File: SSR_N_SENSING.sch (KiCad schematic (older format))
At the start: 15 parts, among them Q1 BC850, U3 ACS722

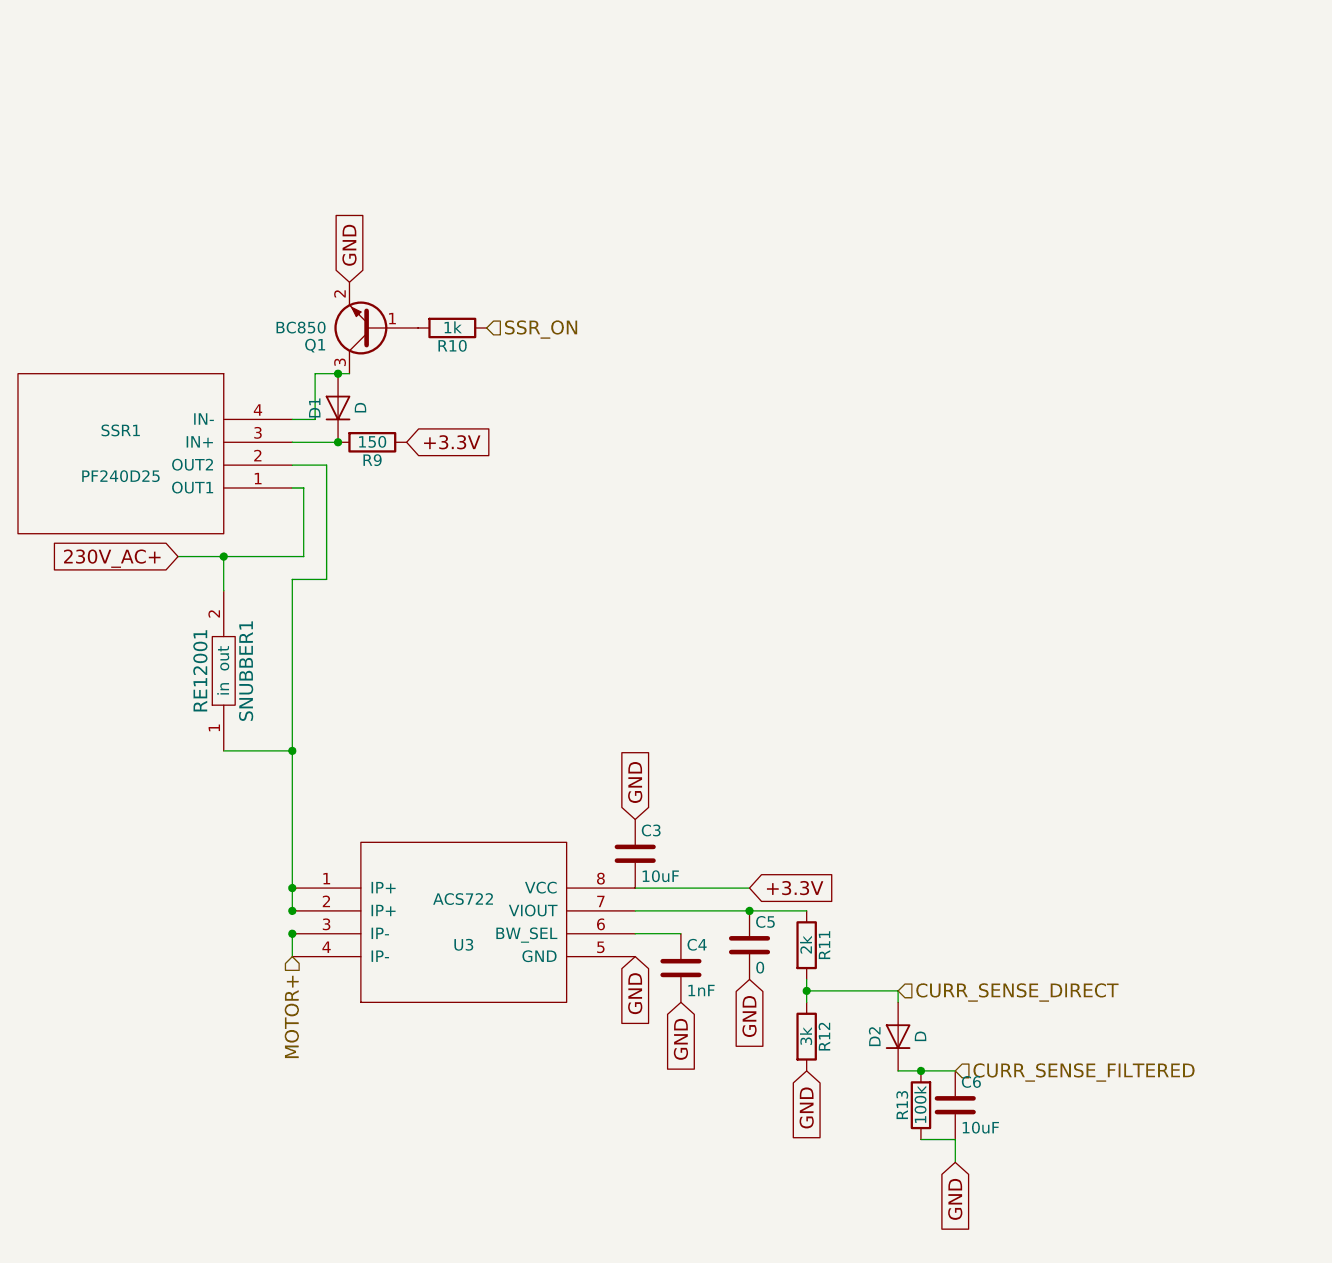
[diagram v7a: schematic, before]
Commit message: before new pcb; - the order of the gpio pins have changed in accordance with olinuxino - indicator leds have been added for debugging - ad current pin added for debugging
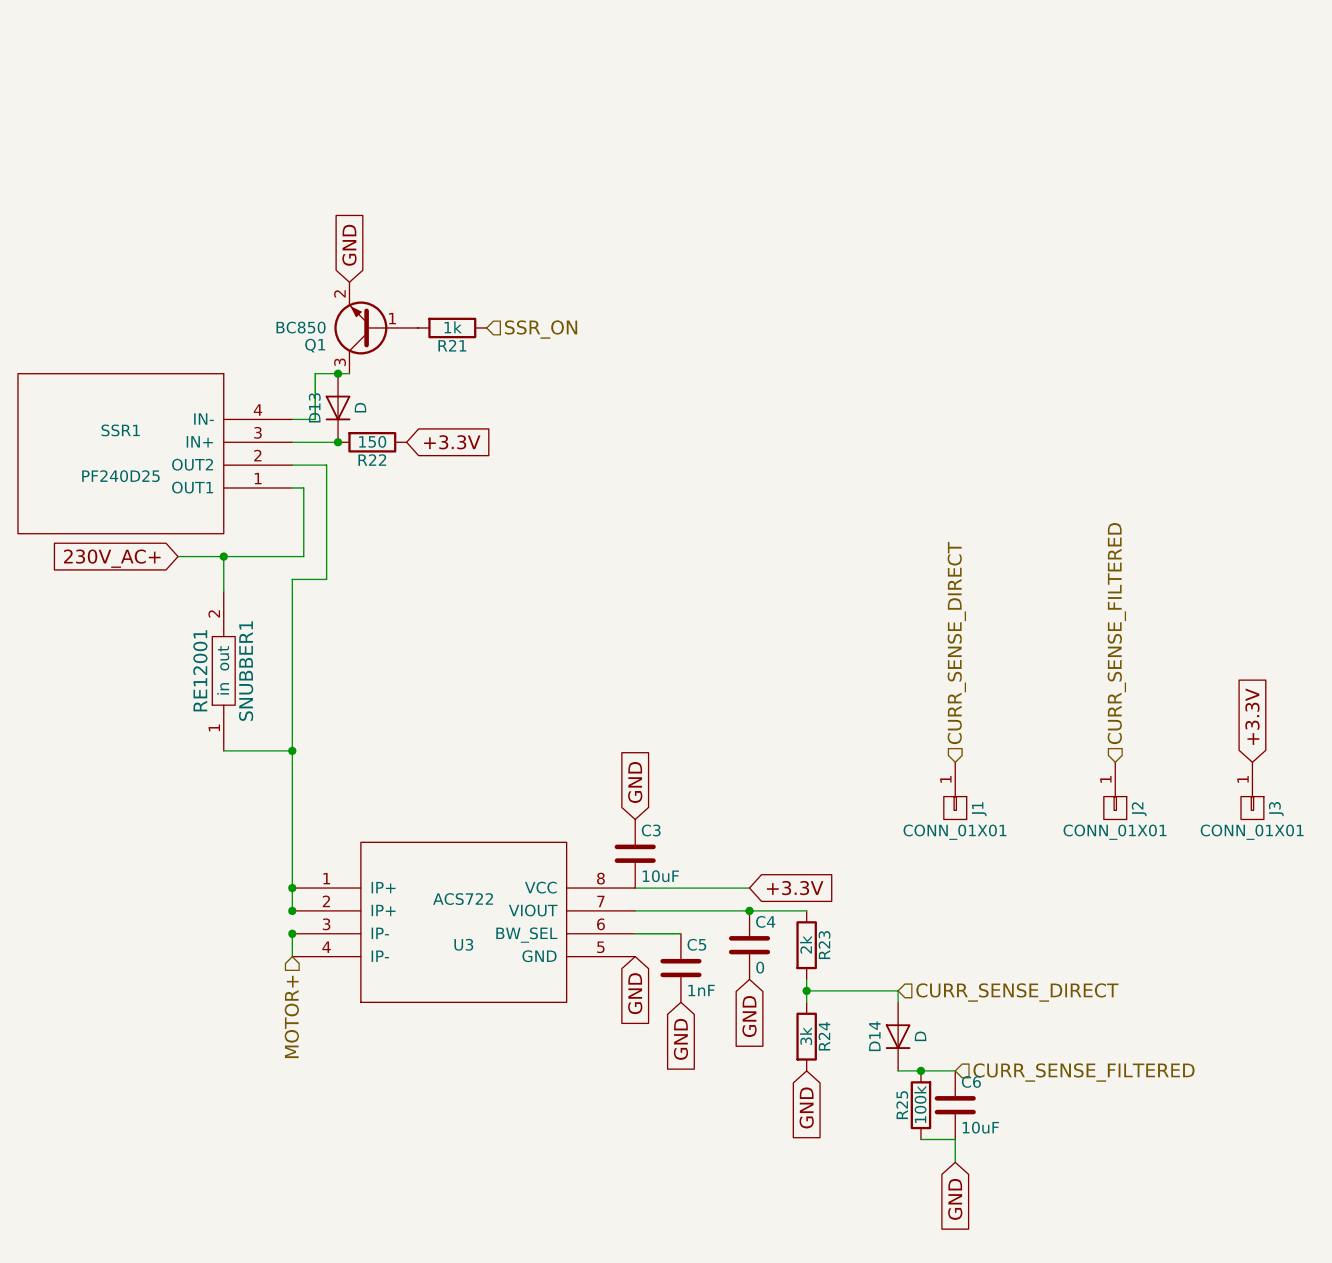
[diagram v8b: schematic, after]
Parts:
- added J1, J2, J3: CONN_01X01, symbol CONN_01X01
- renumbered C5 to C4, C4 to C5, D1 to D13, D2 to D14, R10 to R21, R9 to R22, R11 to R23, R12 to R24, R13 to R25
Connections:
- net +3.3V: now also J3.1 (P1)
- net CURR_SENSE_DIRECT: now also J1.1 (P1)
- net CURR_SENSE_FILTERED: now also J2.1 (P1)
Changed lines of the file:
@@
 MOTOR+
 $Comp
-L D D1
+L D D13
 U 1 1 561BC3FC
 P 3650 2150
-F 0 "D1" H 3650 2250 50  0000 C CNN
+F 0 "D13" H 3650 2250 50  0000 C CNN
 F 1 "D" H 3650 2050 50  0000 C CNN
 F 2 "Diodes_SMD:D_SOD-123" H 3650 2150 60  0001 C CNN
@@
 $EndComp
 $Comp
-L R R9
+L R R22
 U 1 1 561BC4D2
 P 3800 2300
-F 0 "R9" V 3880 2300 50  0000 C CNN
+F 0 "R22" V 3880 2300 50  0000 C CNN
 F 1 "150" V 3800 2300 50  0000 C CNN
 F 2 "Resistors_SMD:R_1206_HandSoldering" V 3730 2300 30  0001 C CNN
@@
 $EndComp
 $Comp
-L R R10
+L R R21
 U 1 1 561BC5DF
 P 4150 1800
-F 0 "R10" V 4230 1800 50  0000 C CNN
+F 0 "R21" V 4230 1800 50  0000 C CNN
 F 1 "1k" V 4150 1800 50  0000 C CNN
 F 2 "Resistors_SMD:R_1206_HandSoldering" V 4080 1800 30  0001 C CNN
@@
 $EndComp
 $Comp
-L C C5
+L C C4
 U 1 1 56251583
 P 5450 4500
-F 0 "C5" H 5475 4600 50  0000 L CNN
+F 0 "C4" H 5475 4600 50  0000 L CNN
 F 1 "0" H 5475 4400 50  0000 L CNN
 F 2 "Capacitors_SMD:C_1206_HandSoldering" H 5488 4350 30  0001 C CNN
@@
 $EndComp
 $Comp
-L D D2
+L D D14
 U 1 1 56251898
 P 6100 4900
-F 0 "D2" H 6100 5000 50  0000 C CNN
+F 0 "D14" H 6100 5000 50  0000 C CNN
 F 1 "D" H 6100 4800 50  0000 C CNN
 F 2 "Diodes_SMD:D_SOD-123" H 6100 4900 60  0001 C CNN
@@
 $EndComp
 $Comp
-L R R13
+L R R25
 U 1 1 5625189E
 P 6200 5200
-F 0 "R13" V 6280 5200 50  0000 C CNN
+F 0 "R25" V 6280 5200 50  0000 C CNN
 F 1 "100k" V 6200 5200 50  0000 C CNN
 F 2 "Resistors_SMD:R_1206_HandSoldering" V 6130 5200 30  0001 C CNN
@@
 CURR_SENSE_FILTERED
 $Comp
-L C C4
+L C C5
 U 1 1 56251AFD
 P 5150 4600
-F 0 "C4" H 5175 4700 50  0000 L CNN
+F 0 "C5" H 5175 4700 50  0000 L CNN
 F 1 "1nF" H 5175 4500 50  0000 L CNN
 F 2 "Capacitors_SMD:C_1206_HandSoldering" H 5188 4450 30  0001 C CNN
@@
 CURR_SENSE_DIRECT
 $Comp
-L R R11
+L R R23
 U 1 1 56255AB8
 P 5700 4500
-F 0 "R11" V 5780 4500 50  0000 C CNN
+F 0 "R23" V 5780 4500 50  0000 C CNN
 F 1 "2k" V 5700 4500 50  0000 C CNN
 F 2 "Resistors_SMD:R_1206_HandSoldering" V 5630 4500 30  0001 C CNN
@@
 $EndComp
 $Comp
-L R R12
+L R R24
 U 1 1 56255B3D
 P 5700 4900
-F 0 "R12" V 5780 4900 50  0000 C CNN
+F 0 "R24" V 5780 4900 50  0000 C CNN
 F 1 "3k" V 5700 4900 50  0000 C CNN
 F 2 "Resistors_SMD:R_1206_HandSoldering" V 5630 4900 30  0001 C CNN
@@
 	3150 3650 3450 3650
 Connection ~ 3450 3650
+$Comp
+L CONN_01X01 J1
+U 1 1 59407490
+P 6350 3900
+F 0 "J1" H 6350 4000 50  0000 C CNN
+F 1 "CONN_01X01" V 6450 3900 50  0000 C CNN
+F 2 "" H 6350 3900 50  0001 C CNN
+F 3 "" H 6350 3900 50  0001 C CNN
+	1    6350 3900
+	0    1    1    0
+$EndComp
+$Comp
+L CONN_01X01 J2
+U 1 1 59407553
+P 7050 3900
+F 0 "J2" H 7050 4000 50  0000 C CNN
+F 1 "CONN_01X01" V 7150 3900 50  0000 C CNN
+F 2 "" H 7050 3900 50  0001 C CNN
+F 3 "" H 7050 3900 50  0001 C CNN
+	1    7050 3900
+	0    1    1    0
+$EndComp
+Text HLabel 6350 3700 1    60   Input ~ 0
+CURR_SENSE_DIRECT
+Text HLabel 7050 3700 1    60   Input ~ 0
+CURR_SENSE_FILTERED
+$Comp
+L CONN_01X01 J3
+U 1 1 59407658
+P 7650 3900
+F 0 "J3" H 7650 4000 50  0000 C CNN
+F 1 "CONN_01X01" V 7750 3900 50  0000 C CNN
+F 2 "" H 7650 3900 50  0001 C CNN
+F 3 "" H 7650 3900 50  0001 C CNN
+	1    7650 3900
+	0    1    1    0
+$EndComp
+Text GLabel 7650 3700 1    60   Input ~ 0
++3.3V
 $EndSCHEMATC
